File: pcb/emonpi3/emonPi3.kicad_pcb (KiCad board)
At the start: 4 copper layers, 85 x 88 mm, 185 parts, among them CN1 CONN_03SCREW, CN2 CONN_03SCREW, CN3 CONN_03SCREW, J1 SJ-3524-SMT-TR, J10 Conn_ARM_JTAG_SWD_10, J11 Conn_02x13_Odd_Even, J12 PINHD-1X9, J2 SJ-3524-SMT-TR, J3 SJ-3524-SMT-TR, J4 SJ-3524-SMT-TR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

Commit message: * Change comparator from LMV331 to MCP6546
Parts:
- U6: value LMV331 -> MCP6456U
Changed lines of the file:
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@@
         (effects (font (size 1 1) (thickness 0.15)))
     )
-    (fp_text value "LMV331" (at 0 2.4 90) (layer "F.Fab")
+    (fp_text value "MCP6456U" (at 0 2.4 90) (layer "F.Fab")
         (effects (font (size 1 1) (thickness 0.15)))
     )

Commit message: * Add power indicator LED to front panel
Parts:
- added LED5: LED, LED_SMD:LED_LiteOn_LTST-S326, F.Cu at (188.8, 134.0)
- added R47: 1K, Resistor_SMD:R_0603_1608Metric, F.Cu at (185.0, 134.5)
- moved C39 2.00 mm to (160.5, 89.5)
- moved C38 1.58 mm to (182.5, 133.5), turned to 90 degrees
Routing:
- net /5V_USB: track 12.2 -> 7.71 mm
- net Net-(LED5-A): track 0.00 -> 2.48 mm
- net +3V3: track 168.1 -> 169.4 mm
- net +5V: track 6.22 -> 7.23 mm
- net GND: vias 115 -> 117
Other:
- board text added: "Ref. Gen."
- board text removed: "Ref. Generator"

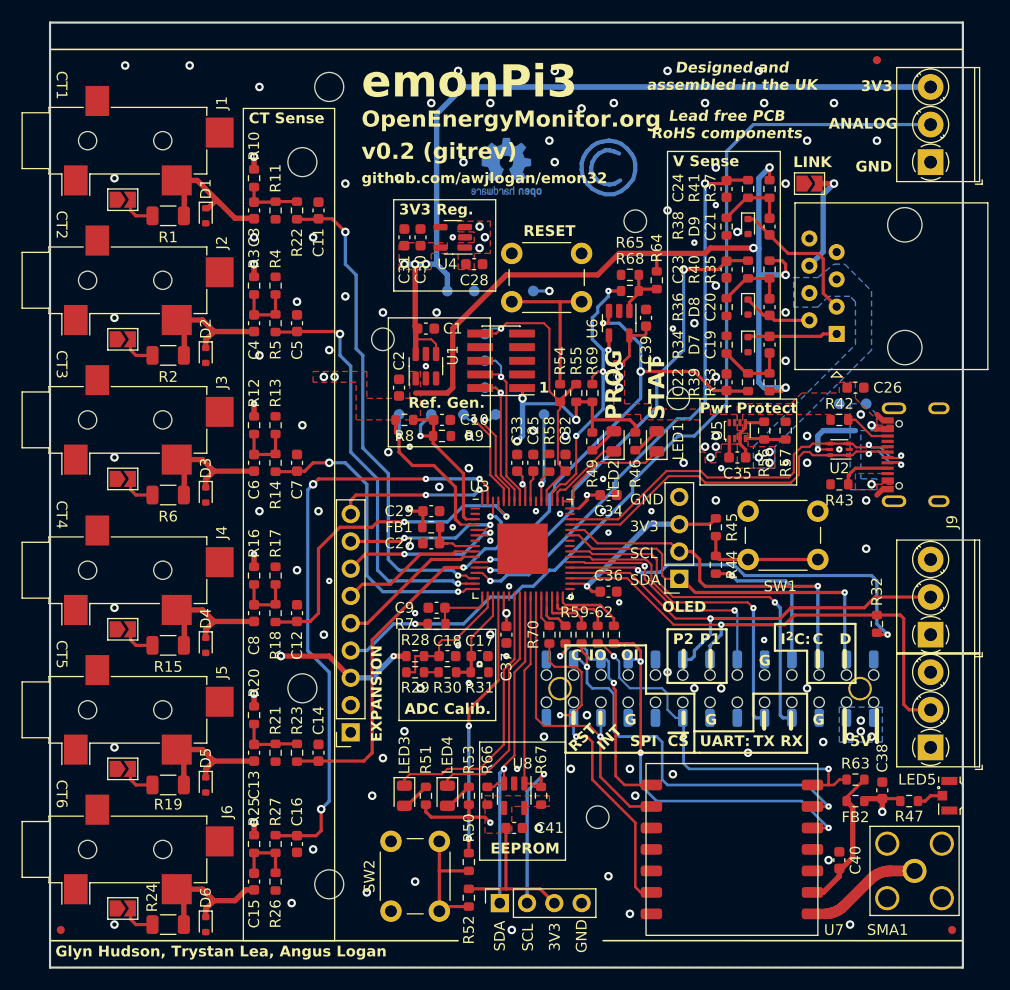
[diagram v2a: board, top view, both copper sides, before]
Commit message: * LED Rationalisation
  - Combine PROG and STATUS as bicolour LED on front panel
  - Mark USER LEDs and switch as DNP, unlikely to be available in
    OEM products.
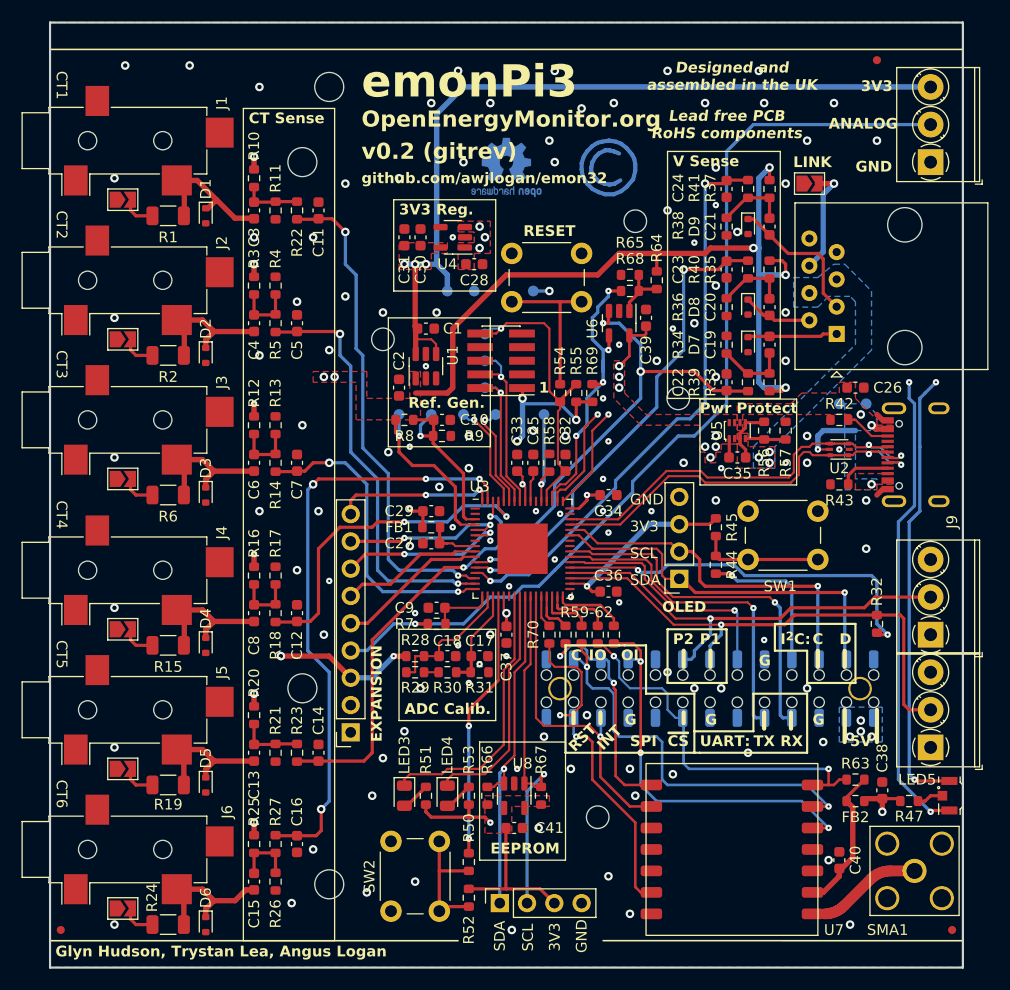
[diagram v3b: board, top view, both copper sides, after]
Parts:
- removed LED1, LED2: Red 1.85V, LED_SMD:LED_0805_2012Metric
- removed R46, R49: 1K, Resistor_SMD:R_0603_1608Metric
- LED5: value LED -> LED_Dual_KAK
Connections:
- LED5 pad 1: GND -> /~{LED_PROG}
- LED5 pad 3: (no net) -> /~{LED_STATUS}
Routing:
- net /~{LED_PROG}: track 7.67 -> 85.5 mm, vias 0 -> 3
- net /~{LED_STATUS}: track 11.3 -> 83.4 mm, vias 0 -> 3
- net +3V3: track 169.4 -> 161.4 mm
- net Net-(LED2-A): track 2.49 -> 0.00 mm
- net Net-(LED1-A): track 2.49 -> 0.00 mm
- net /VSENS_{POL}: track 27.8 -> 29.0 mm
- net /RFM_MOSI: track 37.9 -> 37.2 mm
- net /RFM_SEL: track 35.3 -> 35.0 mm, vias 3 -> 2
- net GND: vias 117 -> 121
- net /~{DISABLE_EXT_INTF}: vias 2 -> 1
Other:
- board text removed: "PROG"
- board text removed: "STAT"

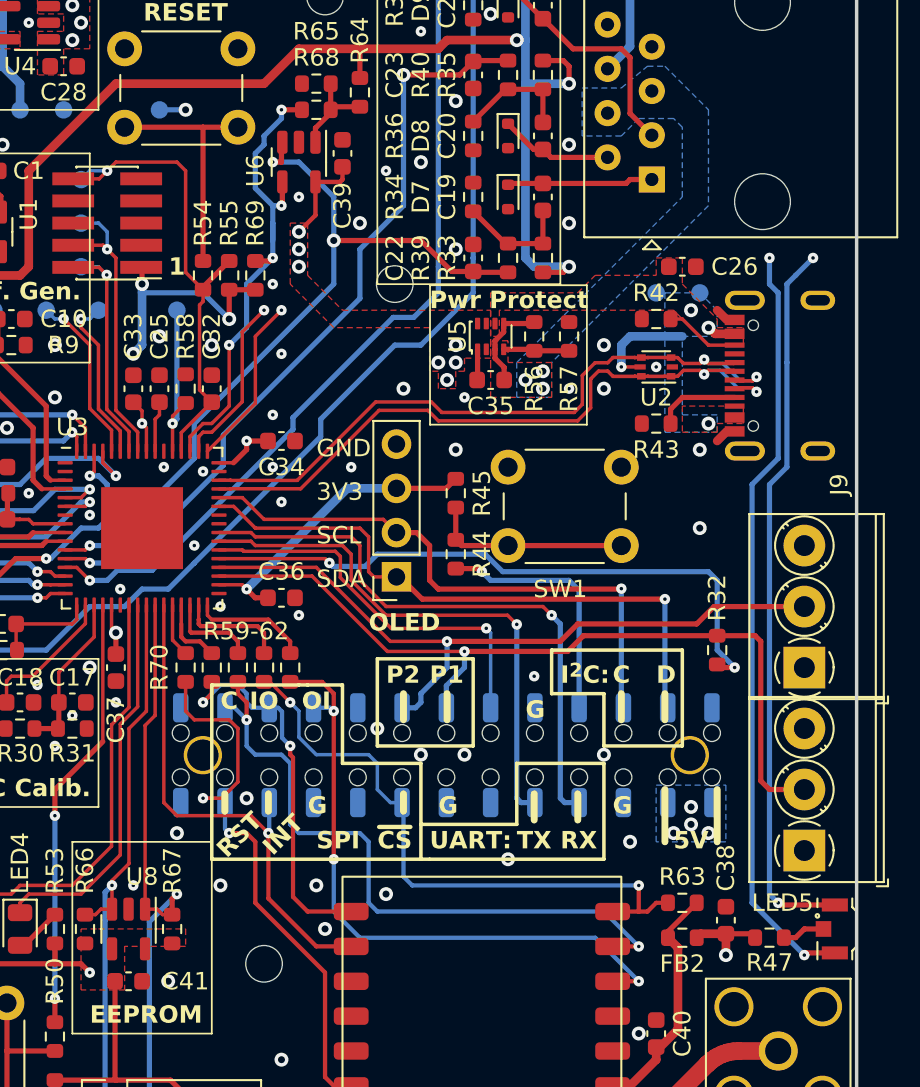
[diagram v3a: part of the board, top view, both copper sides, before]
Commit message: * Expose !RESET to Pi to allow entry to bootloader
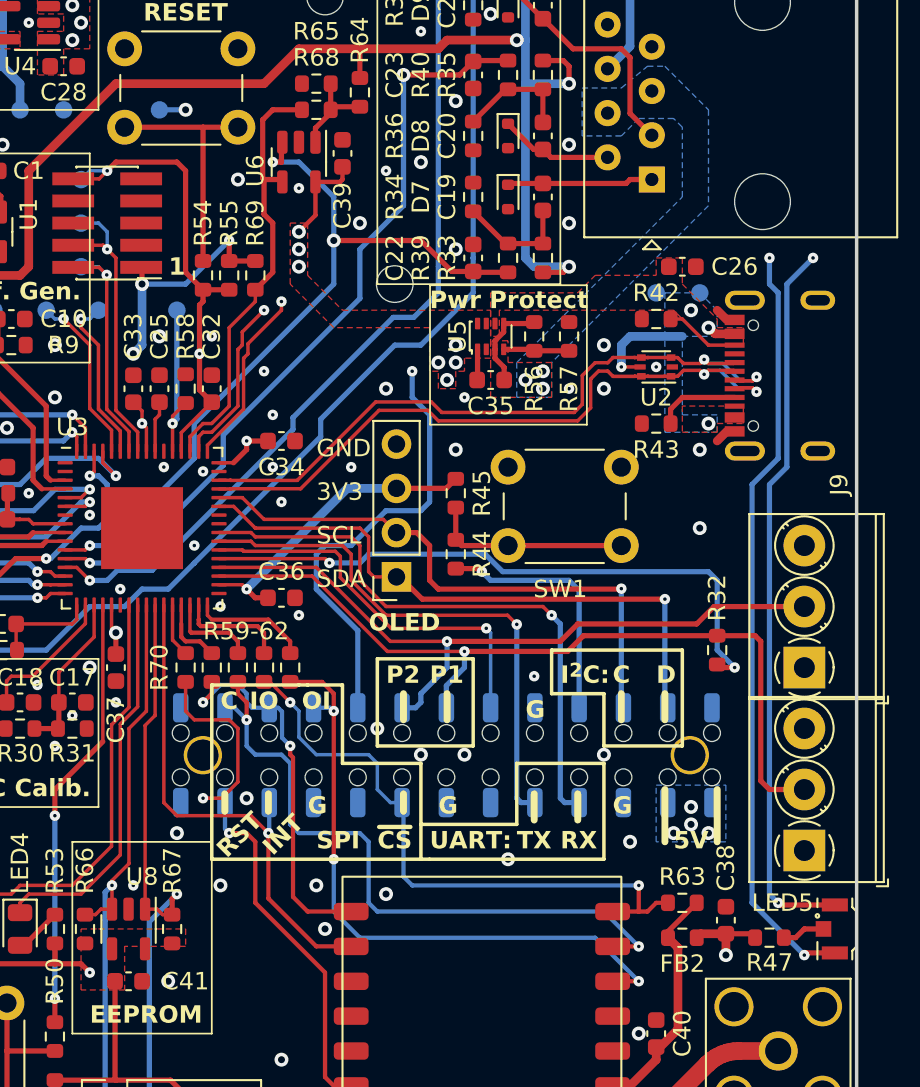
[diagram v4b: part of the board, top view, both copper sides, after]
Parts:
- removed H8: MountingHole, MountingHole:MountingHole_2.1mm
- turned R55 to -90 degrees
- turned R69 to -90 degrees
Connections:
- J11 pad 17: unconnected-(J11-Pin_17-Pad17) -> /~{RESET}
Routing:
- net /~{RESET}: track 28.5 -> 65.9 mm, vias 1 -> 3
- net /VSENS_{POL}: track 29.0 -> 24.9 mm, vias 4 -> 0
